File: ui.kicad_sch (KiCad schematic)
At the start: 45 parts, among them J11 Header_50mil_1x05, J7 Header_100mil_1x06, SW1 PEC11R-4215F-S0024, SW2 PEC11R-4215F-S0024, U10 BL24C256A-SFRC, U11 BME280, U12 SN74HC14PWR, U13 TMP236A4DBZR, U9 SN74AHCT244DBR

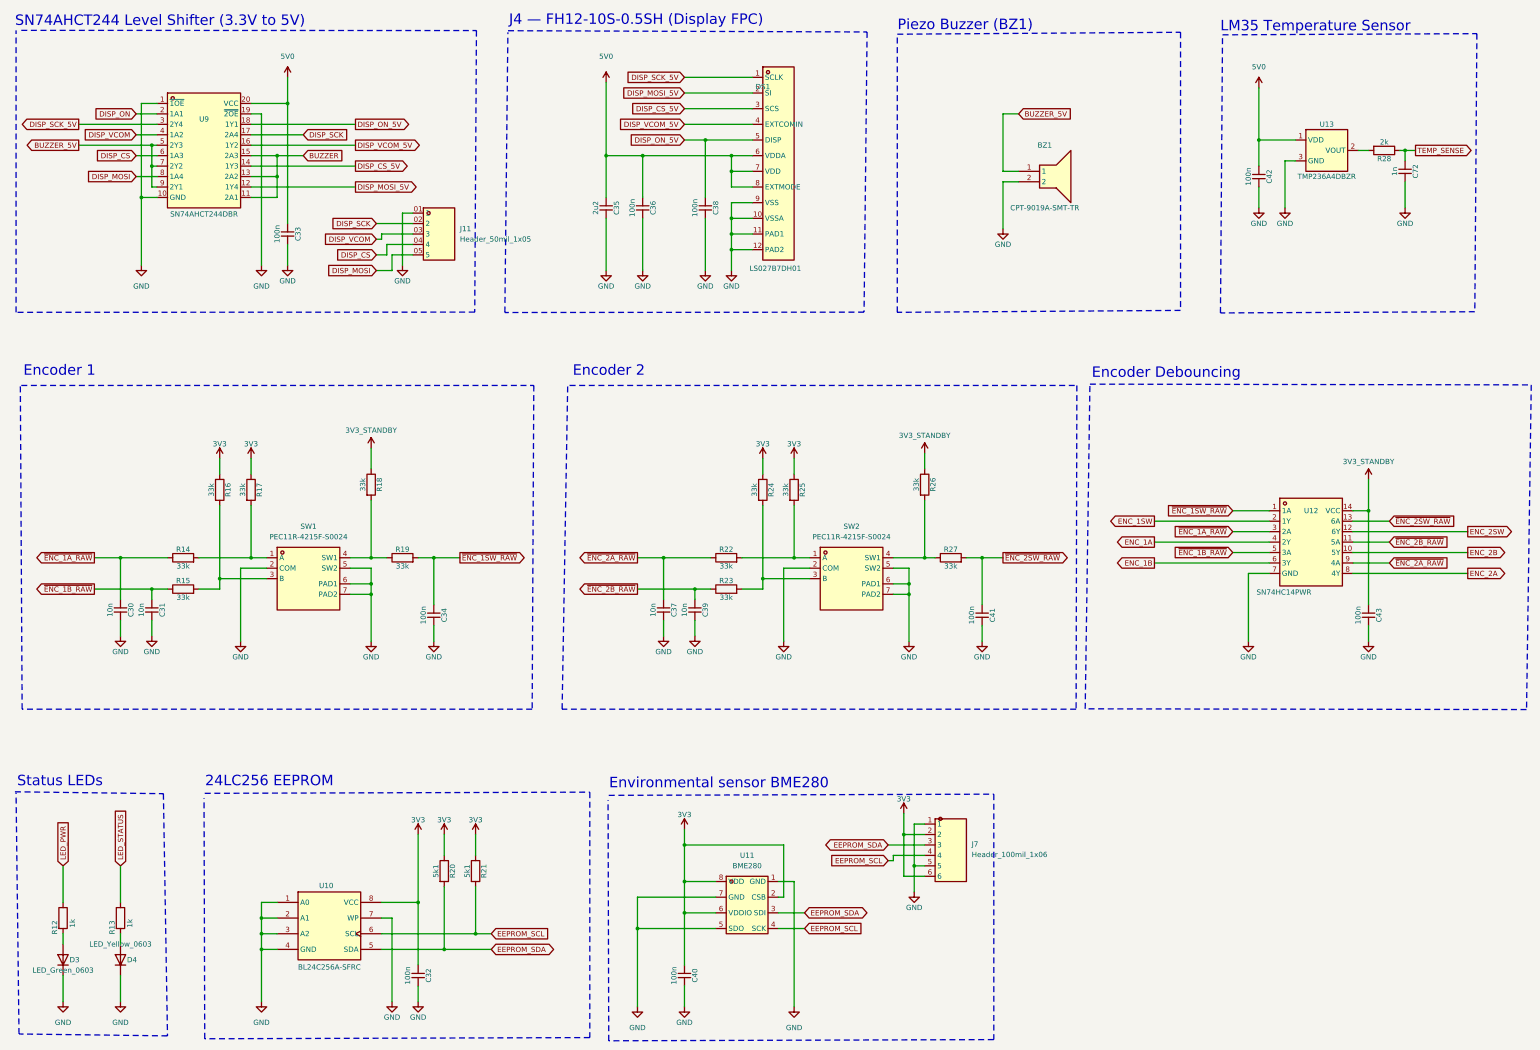
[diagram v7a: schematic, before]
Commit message: LEVELMETER Rev A as ordered
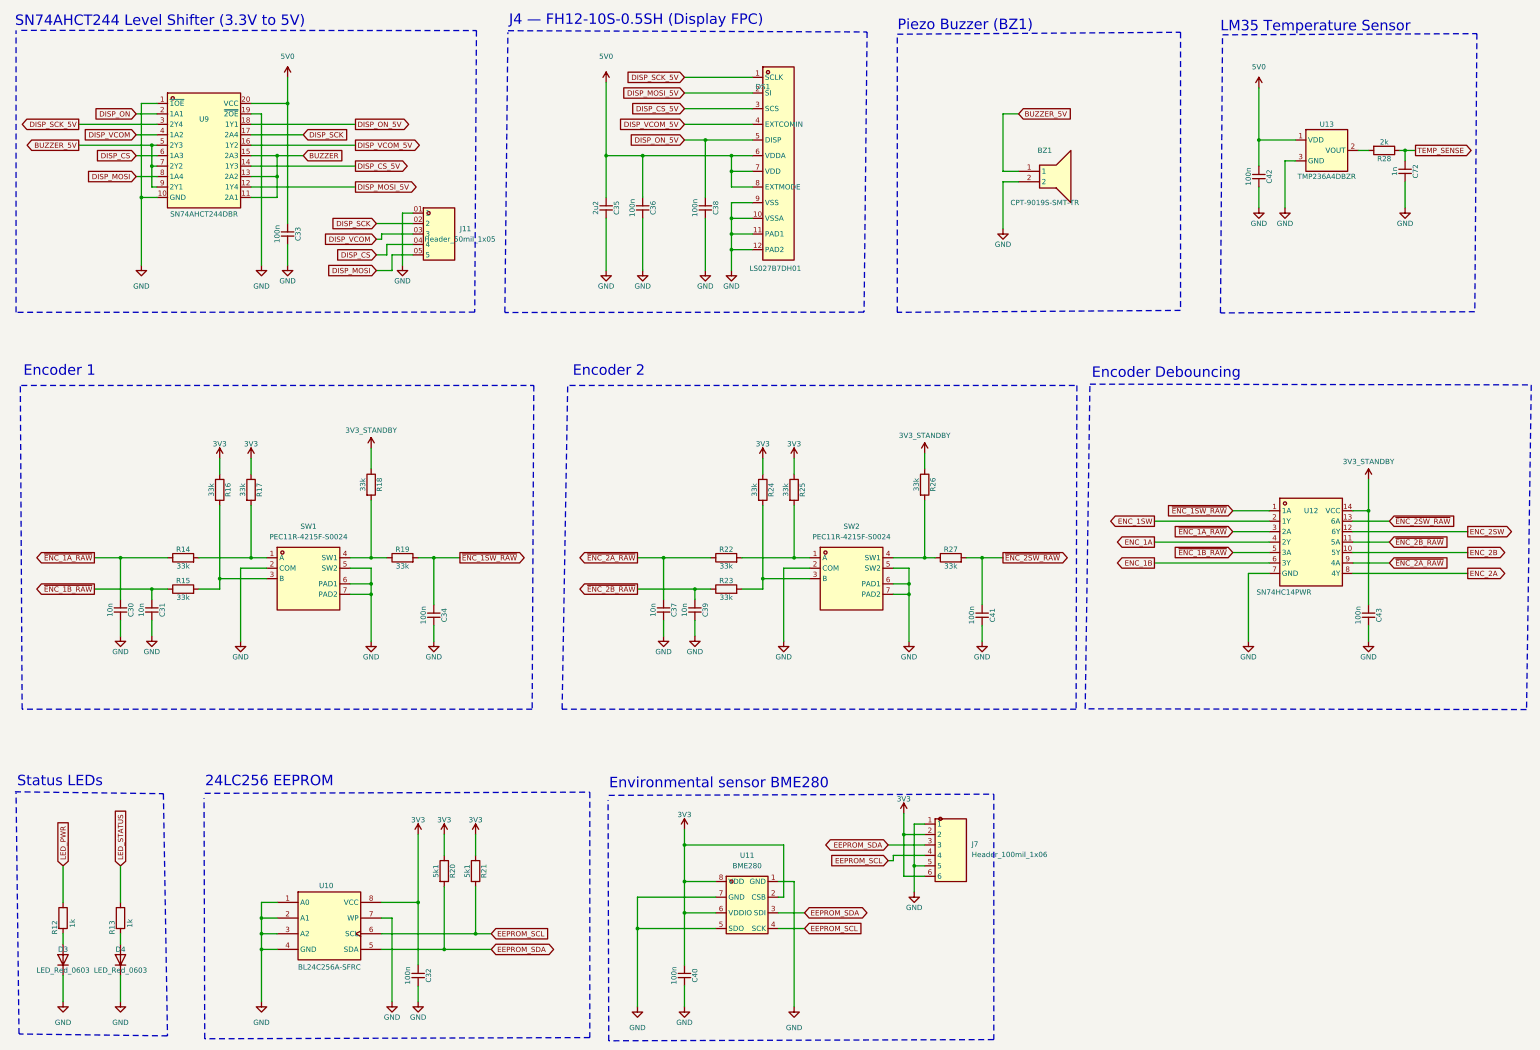
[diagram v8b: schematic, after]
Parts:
- BZ1: value CPT-9019A-SMT-TR -> CPT-9019S-SMT-TR; footprint sldrnrd:CPT-9019A -> sldrnrd:CPT-9019S; symbol sldrnrd:Audio/CPT-9019A-SMT-TR -> sldrnrd:Audio/CPT-9019S-SMT-TR; LCSC C20181991 -> C95163; MPN CPT-9019A-SMT-TR -> CPT-9019S-SMT-TR; Manufacturer CUI -> CUI (Same Sky)
- D3: value LED_Green_0603 -> LED_Red_0603; symbol sldrnrd:LED/LED_Green_0603_NationStar -> sldrnrd:LED/LED_Red_0603; LCSC C87326 -> C2286; MPN NCD0603G2 -> KT-0603R; Manufacturer NationStar -> KENTO
- D4: value LED_Yellow_0603 -> LED_Red_0603; symbol sldrnrd:LED/LED_Yellow_0603 -> sldrnrd:LED/LED_Red_0603; LCSC C2287 -> C2286; MPN KT-0603Y -> KT-0603R
- J11: LCSC C42162999 -> (none); MPN HC-PZ127-7.2L-1x4PZ -> (none); Manufacturer Hong Cheng -> (none)
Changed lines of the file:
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@@
 					(size 1.27 1.27)
 				)
-				(justify left)
 			)
 		)
@@
 			)
 		)
-		(property "Manufacturer" "Hong Cheng"
-			(at 138.43 99.06 0)
-			(hide yes)
-			(show_name no)
-			(do_not_autoplace no)
-			(effects
-				(font
-					(size 1.27 1.27)
-				)
-			)
-		)
-		(property "MPN" "HC-PZ127-7.2L-1x4PZ"
-			(at 138.43 101.6 0)
-			(hide yes)
-			(show_name no)
-			(do_not_autoplace no)
-			(effects
-				(font
-					(size 1.27 1.27)
-				)
-			)
-		)
-		(property "LCSC" "C42162999"
-			(at 138.43 104.14 0)
-			(hide yes)
-			(show_name no)
-			(do_not_autoplace no)
-			(effects
-				(font
-					(size 1.27 1.27)
-				)
-			)
-		)
 		(pin "01"
 		)
@@
 	)
 	(symbol
-		(lib_id "sldrnrd:LED/LED_Green_0603_NationStar")
+		(lib_id "sldrnrd:LED/LED_Red_0603")
 		(at 46.99 260.35 90)
 		(unit 1)
@@
 		(dnp no)
 		(property "Reference" "D3"
-			(at 49.784 260.35 90)
+			(at 46.99 257.81 90)
 			(show_name no)
 			(do_not_autoplace no)
@@
 			)
 		)
-		(property "Value" "LED_Green_0603"
+		(property "Value" "LED_Red_0603"
 			(at 46.99 262.89 90)
 			(show_name no)
@@
 			)
 		)
-		(property "Manufacturer" "NationStar"
+		(property "Manufacturer" "KENTO"
 			(at 46.99 260.35 0)
 			(hide yes)
@@
 			)
 		)
-		(property "MPN" "NCD0603G2"
+		(property "MPN" "KT-0603R"
 			(at 46.99 260.35 0)
 			(hide yes)
@@
 			)
 		)
-		(property "LCSC" "C87326"
+		(property "LCSC" "C2286"
 			(at 46.99 260.35 0)
 			(hide yes)
@@
 	)
 	(symbol
-		(lib_id "sldrnrd:Audio/CPT-9019A-SMT-TR")
+		(lib_id "sldrnrd:Audio/CPT-9019S-SMT-TR")
 		(at 285.75 69.85 0)
 		(unit 1)
@@
 		(dnp no)
 		(property "Reference" "BZ1"
-			(at 285.75 62.23 0)
+			(at 285.75 63.5 0)
 			(show_name no)
 			(do_not_autoplace no)
@@
 			)
 		)
-		(property "Value" "CPT-9019A-SMT-TR"
-			(at 285.75 77.47 0)
+		(property "Value" "CPT-9019S-SMT-TR"
+			(at 285.75 76.2 0)
 			(show_name no)
 			(do_not_autoplace no)
@@
 			)
 		)
-		(property "Footprint" "sldrnrd:CPT-9019A"
+		(property "Footprint" "sldrnrd:CPT-9019S"
 			(at 285.75 78.74 0)
 			(hide yes)
@@
 			)
 		)
-		(property "Datasheet" "${SLDRNRD_LIB}/datasheets/Audio/CPT-9019A.pdf"
+		(property "Datasheet" "${SLDRNRD_LIB}/datasheets/Audio/CPT-9019S-SMT-TR.pdf"
 			(at 285.75 81.28 0)
 			(hide yes)
@@
 			)
 		)
-		(property "Manufacturer" "CUI"
+		(property "Manufacturer" "CUI (Same Sky)"
 			(at 285.75 83.82 0)
 			(hide yes)
@@
 			)
 		)
-		(property "MPN" "CPT-9019A-SMT-TR"
+		(property "MPN" "CPT-9019S-SMT-TR"
 			(at 285.75 86.36 0)
 			(hide yes)
@@
 			)
 		)
-		(property "LCSC" "C20181991"
+		(property "LCSC" "C95163"
 			(at 285.75 88.9 0)
 			(hide yes)
@@
 	)
 	(symbol
-		(lib_id "sldrnrd:LED/LED_Yellow_0603")
+		(lib_id "sldrnrd:LED/LED_Red_0603")
 		(at 60.96 260.35 90)
 		(unit 1)
@@
 		(dnp no)
 		(property "Reference" "D4"
-			(at 63.754 260.35 90)
+			(at 60.96 257.81 90)
 			(show_name no)
 			(do_not_autoplace no)
@@
 			)
 		)
-		(property "Value" "LED_Yellow_0603"
-			(at 60.96 256.54 90)
+		(property "Value" "LED_Red_0603"
+			(at 60.96 262.89 90)
 			(show_name no)
 			(do_not_autoplace no)
@@
 			)
 		)
-		(property "MPN" "KT-0603Y"
+		(property "MPN" "KT-0603R"
 			(at 60.96 260.35 0)
 			(hide yes)
@@
 			)
 		)
-		(property "LCSC" "C2287"
+		(property "LCSC" "C2286"
 			(at 60.96 260.35 0)
 			(hide yes)
@@
 		)
 	)
-	(embedded_fonts no)
 )
